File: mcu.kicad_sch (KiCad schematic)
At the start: 13 parts, among them U6 ATtiny3217

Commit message: Added labels and schematic PDF among other progress
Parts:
- U6: footprint Package_SO:TSSOP-20_4.4x6.5mm_P0.65mm -> Package_DFN_QFN:QFN-24-1EP_4x4mm_P0.5mm_EP2.6x2.6mm
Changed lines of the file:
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@@
 			)
 		)
-		(property "Footprint" "Package_SO:TSSOP-20_4.4x6.5mm_P0.65mm"
+		(property "Footprint" "Package_DFN_QFN:QFN-24-1EP_4x4mm_P0.5mm_EP2.6x2.6mm"
 			(at 133.35 133.35 0)
 			(hide yes)

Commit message: Added testpoints
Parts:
- added TP32: MCU_VCC, symbol Connector:TestPoint_Small
- renumbered C13 to C14, C14 to C15, R36 to R30, R38 to R31, R37 to R32, R30 to R33, R31 to R34, R32 to R35, R33 to R36, R34 to R37, R35 to R38, TP19 to TP33
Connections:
- net MCU_VCC: now also TP32.1
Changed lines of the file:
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@@
+	)
+	(junction
+		(at 133.35 82.55)
+		(diameter 0)
+		(color 0 0 0 0)
 	)
 	(junction
@@
 		(effects
 			(font
-				(size 1.27 1.27)
+				(size 1 1)
+				(thickness 0.254)
+				(bold yes)
 			)
 			(justify right bottom)
@@
 		(effects
 			(font
-				(size 1.27 1.27)
+				(size 1 1)
+				(thickness 0.2)
+				(bold yes)
 			)
 			(justify left bottom)
@@
 		(effects
 			(font
-				(size 1.27 1.27)
+				(size 1 1)
+				(thickness 0.2)
+				(bold yes)
 			)
 			(justify right bottom)
@@
 			(font
 				(size 1 1)
+				(thickness 0.2)
+				(bold yes)
 			)
 			(justify left bottom)
@@
 			(font
 				(size 1 1)
+				(thickness 0.2)
+				(bold yes)
 			)
 			(justify left bottom)
@@
 		(effects
 			(font
-				(size 1.27 1.27)
+				(size 1 1)
+				(thickness 0.2)
+				(bold yes)
 			)
 			(justify left bottom)
@@
 			(font
 				(size 1 1)
+				(thickness 0.2)
+				(bold yes)
 			)
 			(justify right bottom)
@@
 		(in_pos_files yes)
 		(dnp no)
-		(property "Reference" "R30"
+		(property "Reference" "R33"
 			(at 178.816 66.04 90)
 			(show_name no)
@@
 			(project "power_module"
 				(path "/33e2b92e-f705-4be7-96f4-57092b8ec1ea/20438595-580a-4bb7-878e-f4267085e0b4"
-					(reference "R30")
+					(reference "R33")
 					(unit 1)
 				)
@@
 		(in_pos_files yes)
 		(dnp no)
-		(property "Reference" "R37"
+		(property "Reference" "R32"
 			(at 180.34 127.254 0)
 			(show_name no)
@@
 			(project "power_module"
 				(path "/33e2b92e-f705-4be7-96f4-57092b8ec1ea/20438595-580a-4bb7-878e-f4267085e0b4"
-					(reference "R37")
+					(reference "R32")
 					(unit 1)
 				)
@@
 		(in_pos_files yes)
 		(dnp no)
-		(property "Reference" "C14"
+		(property "Reference" "C15"
 			(at 100.838 80.518 0)
 			(show_name no)
@@
 			(project "power_module"
 				(path "/33e2b92e-f705-4be7-96f4-57092b8ec1ea/20438595-580a-4bb7-878e-f4267085e0b4"
-					(reference "C14")
+					(reference "C15")
 					(unit 1)
 				)
@@
 		(in_pos_files yes)
 		(dnp no)
-		(property "Reference" "R33"
+		(property "Reference" "R36"
 			(at 179.578 84.836 90)
 			(show_name no)
@@
 			(project "power_module"
 				(path "/33e2b92e-f705-4be7-96f4-57092b8ec1ea/20438595-580a-4bb7-878e-f4267085e0b4"
-					(reference "R33")
+					(reference "R36")
 					(unit 1)
 				)
@@
 		(in_pos_files yes)
 		(dnp no)
-		(property "Reference" "R38"
+		(property "Reference" "R31"
 			(at 151.13 86.106 90)
 			(show_name no)
@@
 			(project "power_module"
 				(path "/33e2b92e-f705-4be7-96f4-57092b8ec1ea/20438595-580a-4bb7-878e-f4267085e0b4"
-					(reference "R38")
+					(reference "R31")
 					(unit 1)
 				)
@@
 		(in_pos_files yes)
 		(dnp no)
-		(property "Reference" "R35"
+		(property "Reference" "R38"
 			(at 179.832 100.076 90)
 			(show_name no)
@@
 			(project "power_module"
 				(path "/33e2b92e-f705-4be7-96f4-57092b8ec1ea/20438595-580a-4bb7-878e-f4267085e0b4"
-					(reference "R35")
+					(reference "R38")
 					(unit 1)
 				)
@@
 		(in_pos_files yes)
 		(dnp no)
-		(property "Reference" "TP19"
+		(property "Reference" "TP33"
 			(at 183.896 130.302 90)
 			(show_name no)
@@
 			(project "power_module"
 				(path "/33e2b92e-f705-4be7-96f4-57092b8ec1ea/20438595-580a-4bb7-878e-f4267085e0b4"
-					(reference "TP19")
+					(reference "TP33")
 					(unit 1)
 				)
@@
 		(in_pos_files yes)
 		(dnp no)
-		(property "Reference" "#PWR038"
+		(property "Reference" "#PWR040"
 			(at 91.44 91.44 0)
 			(hide yes)
@@
 			(project "power_module"
 				(path "/33e2b92e-f705-4be7-96f4-57092b8ec1ea/20438595-580a-4bb7-878e-f4267085e0b4"
-					(reference "#PWR038")
+					(reference "#PWR040")
 					(unit 1)
 				)
@@
 		(in_pos_files yes)
 		(dnp no)
-		(property "Reference" "C13"
+		(property "Reference" "C14"
 			(at 85.852 80.518 0)
 			(show_name no)
@@
 			(project "power_module"
 				(path "/33e2b92e-f705-4be7-96f4-57092b8ec1ea/20438595-580a-4bb7-878e-f4267085e0b4"
-					(reference "C13")
+					(reference "C14")
 					(unit 1)
 				)
@@
 		(in_pos_files yes)
 		(dnp no)
-		(property "Reference" "#PWR036"
+		(property "Reference" "#PWR041"
 			(at 133.35 78.74 0)
 			(hide yes)
@@
 			(project "power_module"
 				(path "/33e2b92e-f705-4be7-96f4-57092b8ec1ea/20438595-580a-4bb7-878e-f4267085e0b4"
-					(reference "#PWR036")
+					(reference "#PWR041")
 					(unit 1)
 				)
@@
 		(in_pos_files yes)
 		(dnp no)
-		(property "Reference" "R31"
+		(property "Reference" "R34"
 			(at 178.816 72.39 90)
 			(show_name no)
@@
 			(project "power_module"
 				(path "/33e2b92e-f705-4be7-96f4-57092b8ec1ea/20438595-580a-4bb7-878e-f4267085e0b4"
-					(reference "R31")
+					(reference "R34")
 					(unit 1)
 				)
@@
 		(in_pos_files yes)
 		(dnp no)
-		(property "Reference" "R34"
+		(property "Reference" "R37"
 			(at 179.578 91.186 90)
 			(show_name no)
@@
 			(project "power_module"
 				(path "/33e2b92e-f705-4be7-96f4-57092b8ec1ea/20438595-580a-4bb7-878e-f4267085e0b4"
-					(reference "R34")
+					(reference "R37")
+					(unit 1)
+				)
+			)
+		)
+	)
+	(symbol
+		(lib_id "Connector:TestPoint_Small")
+		(at 133.35 82.55 0)
+		(unit 1)
+		(body_style 1)
+		(exclude_from_sim no)
+		(in_bom yes)
+		(on_board yes)
+		(in_pos_files yes)
+		(dnp no)
+		(property "Reference" "TP32"
+			(at 133.858 82.042 0)
+			(show_name no)
+			(do_not_autoplace no)
+			(effects
+				(font
+					(size 1.27 1.27)
+				)
+				(justify left)
+			)
+		)
+		(property "Value" "MCU_VCC"
+			(at 134.62 83.8199 0)
+			(hide yes)
+			(show_name no)
+			(do_not_autoplace no)
+			(effects
+				(font
+					(size 1.27 1.27)
+				)
+				(justify left)
+			)
+		)
+		(property "Footprint" ""
+			(at 138.43 82.55 0)
+			(hide yes)
+			(show_name no)
+			(do_not_autoplace no)
+			(effects
+				(font
+					(size 1.27 1.27)
+				)
+			)
+		)
+		(property "Datasheet" ""
+			(at 138.43 82.55 0)
+			(hide yes)
+			(show_name no)
+			(do_not_autoplace no)
+			(effects
+				(font
+					(size 1.27 1.27)
+				)
+			)
+		)
+		(property "Description" "test point"
+			(at 133.35 82.55 0)
+			(hide yes)
+			(show_name no)
+			(do_not_autoplace no)
+			(effects
+				(font
+					(size 1.27 1.27)
+				)
+			)
+		)
+		(pin "1"
+		)
+		(instances
+			(project "power_module"
+				(path "/33e2b92e-f705-4be7-96f4-57092b8ec1ea/20438595-580a-4bb7-878e-f4267085e0b4"
+					(reference "TP32")
 					(unit 1)
 				)
@@
 		(in_pos_files yes)
 		(dnp no)
-		(property "Reference" "R32"
+		(property "Reference" "R35"
 			(at 179.324 80.772 90)
 			(show_name no)
@@
 			(project "power_module"
 				(path "/33e2b92e-f705-4be7-96f4-57092b8ec1ea/20438595-580a-4bb7-878e-f4267085e0b4"
-					(reference "R32")
+					(reference "R35")
 					(unit 1)
 				)
@@
 		(in_pos_files yes)
 		(dnp no)
-		(property "Reference" "#PWR037"
+		(property "Reference" "#PWR042"
 			(at 133.35 144.78 0)
 			(hide yes)
@@
 			(project "power_module"
 				(path "/33e2b92e-f705-4be7-96f4-57092b8ec1ea/20438595-580a-4bb7-878e-f4267085e0b4"
-					(reference "#PWR037")
+					(reference "#PWR042")
 					(unit 1)
 				)
@@
 		(in_pos_files yes)
 		(dnp no)
-		(property "Reference" "R36"
+		(property "Reference" "R30"
 			(at 132.334 77.216 0)
 			(show_name no)
@@
 			(project "power_module"
 				(path "/33e2b92e-f705-4be7-96f4-57092b8ec1ea/20438595-580a-4bb7-878e-f4267085e0b4"
-					(reference "R36")
+					(reference "R30")
 					(unit 1)
 				)

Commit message: Partially assigned netclasses WIP
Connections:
- net UDPI renamed UPDI
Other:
- moved on the sheet: R31
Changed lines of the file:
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@@
+	)
+	(junction
+		(at 175.26 132.08)
+		(diameter 0)
+		(color 0 0 0 0)
 	)
 	(junction
@@
 	)
 	(junction
-		(at 175.26 132.08)
-		(diameter 0)
-		(color 0 0 0 0)
-	)
-	(junction
 		(at 185.42 78.74)
 		(diameter 0)
@@
 	(wire
 		(pts
-			(xy 148.59 90.17) (xy 149.86 90.17)
+			(xy 148.59 90.17) (xy 151.13 90.17)
 		)
 		(stroke
@@
 		(pts
 			(xy 185.42 69.85) (xy 185.42 76.2)
-		)
-		(stroke
-			(width 0)
-			(type default)
-		)
-	)
-	(wire
-		(pts
-			(xy 157.48 90.17) (xy 158.75 90.17)
 		)
 		(stroke
@@
 		)
 	)
-	(hierarchical_label "UDPI"
+	(hierarchical_label "UPDI"
 		(shape bidirectional)
 		(at 158.75 90.17 0)
@@
 	(symbol
 		(lib_id "Device:R_US")
-		(at 153.67 90.17 90)
+		(at 154.94 90.17 90)
 		(mirror x)
 		(unit 1)
@@
 		(dnp no)
 		(property "Reference" "R31"
-			(at 151.13 86.106 90)
+			(at 152.4 86.106 90)
 			(show_name no)
 			(do_not_autoplace no)
@@
 		)
 		(property "Value" "100R"
-			(at 151.384 88.138 90)
+			(at 152.654 88.138 90)
 			(show_name no)
 			(do_not_autoplace no)
@@
 		)
 		(property "Footprint" "Resistor_SMD:R_0603_1608Metric"
-			(at 153.924 91.186 90)
+			(at 155.194 91.186 90)
 			(hide yes)
 			(show_name no)
@@
 		)
 		(property "Datasheet" ""
-			(at 153.67 90.17 0)
+			(at 154.94 90.17 0)
 			(hide yes)
 			(show_name no)
@@
 		)
 		(property "Description" "Resistor, US symbol"
-			(at 153.67 90.17 0)
+			(at 154.94 90.17 0)
 			(hide yes)
 			(show_name no)
@@
 		)
 		(property "MFR#" "RC0603FR-07100RL"
-			(at 153.67 90.17 0)
+			(at 154.94 90.17 0)
 			(hide yes)
 			(show_name no)
@@
 		)
 		(property "Package" "0603"
-			(at 153.67 90.17 0)
+			(at 154.94 90.17 0)
 			(hide yes)
 			(show_name no)
@@
 		)
 		(property "LCSC#" "C105588"
-			(at 153.67 90.17 0)
-			(hide yes)
-			(show_name no)
+			(at 154.94 90.17 0)
+			(hide yes)
+			(show_name no)

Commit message: Configured Varients
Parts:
- renumbered R30 to R31, R31 to R32, R32 to R33, R33 to R34, R34 to R35, R35 to R36, R36 to R37, R37 to R38, R38 to R39
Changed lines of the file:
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@@
 		(in_pos_files yes)
 		(dnp no)
-		(property "Reference" "R33"
+		(property "Reference" "R34"
 			(at 178.816 66.04 90)
 			(show_name no)
@@
 			(project "power_module"
 				(path "/33e2b92e-f705-4be7-96f4-57092b8ec1ea/20438595-580a-4bb7-878e-f4267085e0b4"
-					(reference "R33")
+					(reference "R34")
 					(unit 1)
+					(variant
+						(name "3v3 Dumb")
+						(dnp yes)
+					)
+					(variant
+						(name "5v Dumb")
+						(dnp yes)
+					)
 				)
 			)
@@
 		(in_pos_files yes)
 		(dnp no)
-		(property "Reference" "R32"
+		(property "Reference" "R33"
 			(at 180.34 127.254 0)
 			(show_name no)
@@
 			(project "power_module"
 				(path "/33e2b92e-f705-4be7-96f4-57092b8ec1ea/20438595-580a-4bb7-878e-f4267085e0b4"
-					(reference "R32")
+					(reference "R33")
 					(unit 1)
+					(variant
+						(name "3v3 Dumb")
+						(dnp yes)
+					)
+					(variant
+						(name "5v Dumb")
+						(dnp yes)
+					)
 				)
 			)
@@
 					(reference "C15")
 					(unit 1)
+					(variant
+						(name "3v3 Dumb")
+						(dnp yes)
+					)
+					(variant
+						(name "5v Dumb")
+						(dnp yes)
+					)
 				)
 			)
@@
 		(in_pos_files yes)
 		(dnp no)
-		(property "Reference" "R36"
+		(property "Reference" "R37"
 			(at 179.578 84.836 90)
 			(show_name no)
@@
 			(project "power_module"
 				(path "/33e2b92e-f705-4be7-96f4-57092b8ec1ea/20438595-580a-4bb7-878e-f4267085e0b4"
-					(reference "R36")
+					(reference "R37")
 					(unit 1)
+					(variant
+						(name "3v3 Dumb")
+						(dnp yes)
+					)
+					(variant
+						(name "5v Dumb")
+						(dnp yes)
+					)
 				)
 			)
@@
 		(in_pos_files yes)
 		(dnp no)
-		(property "Reference" "R31"
+		(property "Reference" "R32"
 			(at 152.4 86.106 90)
 			(show_name no)
@@
 			(project "power_module"
 				(path "/33e2b92e-f705-4be7-96f4-57092b8ec1ea/20438595-580a-4bb7-878e-f4267085e0b4"
-					(reference "R31")
+					(reference "R32")
 					(unit 1)
 				)
@@
 		(in_pos_files yes)
 		(dnp no)
-		(property "Reference" "R38"
+		(property "Reference" "R39"
 			(at 179.832 100.076 90)
 			(show_name no)
@@
 			(project "power_module"
 				(path "/33e2b92e-f705-4be7-96f4-57092b8ec1ea/20438595-580a-4bb7-878e-f4267085e0b4"
-					(reference "R38")
+					(reference "R39")
 					(unit 1)
+					(variant
+						(name "3v3 Dumb")
+						(dnp yes)
+					)
+					(variant
+						(name "5v Dumb")
+						(dnp yes)
+					)
 				)
 			)
@@
 					(reference "C14")
 					(unit 1)
+					(variant
+						(name "3v3 Dumb")
+						(dnp yes)
+					)
+					(variant
+						(name "5v Dumb")
+						(dnp yes)
+					)
 				)
 			)
@@
 		(in_pos_files yes)
 		(dnp no)
-		(property "Reference" "R34"
+		(property "Reference" "R35"
 			(at 178.816 72.39 90)
 			(show_name no)
@@
 			(project "power_module"
 				(path "/33e2b92e-f705-4be7-96f4-57092b8ec1ea/20438595-580a-4bb7-878e-f4267085e0b4"
-					(reference "R34")
+					(reference "R35")
 					(unit 1)
+					(variant
+						(name "3v3 Dumb")
+						(dnp yes)
+					)
+					(variant
+						(name "5v Dumb")
+						(dnp yes)
+					)
 				)
 			)
@@
 		(in_pos_files yes)
 		(dnp no)
-		(property "Reference" "R37"
+		(property "Reference" "R38"
 			(at 179.578 91.186 90)
 			(show_name no)
@@
 			(project "power_module"
 				(path "/33e2b92e-f705-4be7-96f4-57092b8ec1ea/20438595-580a-4bb7-878e-f4267085e0b4"
-					(reference "R37")
+					(reference "R38")
 					(unit 1)
+					(variant
+						(name "3v3 Dumb")
+						(dnp yes)
+					)
+					(variant
+						(name "5v Dumb")
+						(dnp yes)
+					)
 				)
 			)
@@
 		(in_pos_files yes)
 		(dnp no)
-		(property "Reference" "R35"
+		(property "Reference" "R36"
 			(at 179.324 80.772 90)
 			(show_name no)
@@
 			(project "power_module"
 				(path "/33e2b92e-f705-4be7-96f4-57092b8ec1ea/20438595-580a-4bb7-878e-f4267085e0b4"
-					(reference "R35")
+					(reference "R36")
 					(unit 1)
+					(variant
+						(name "3v3 Dumb")
+						(dnp yes)
+					)
+					(variant
+						(name "5v Dumb")
+						(dnp yes)
+					)
 				)
 			)
@@
 		(in_pos_files yes)
 		(dnp no)
-		(property "Reference" "R30"
+		(property "Reference" "R31"
 			(at 132.334 77.216 0)
 			(show_name no)
@@
 			(project "power_module"
 				(path "/33e2b92e-f705-4be7-96f4-57092b8ec1ea/20438595-580a-4bb7-878e-f4267085e0b4"
-					(reference "R30")
+					(reference "R31")
 					(unit 1)
+					(variant
+						(name "3v3 Dumb")
+						(dnp yes)
+					)
+					(variant
+						(name "5v Dumb")
+						(dnp yes)
+					)
 				)
 			)
@@
 					(reference "U6")
 					(unit 1)
-				)
-			)
+					(variant
+						(name "3v3 Dumb")
+						(dnp yes)
+					)
+					(variant
+						(name "5v Dumb")
+						(dnp yes)
+					)
+				)
+			)

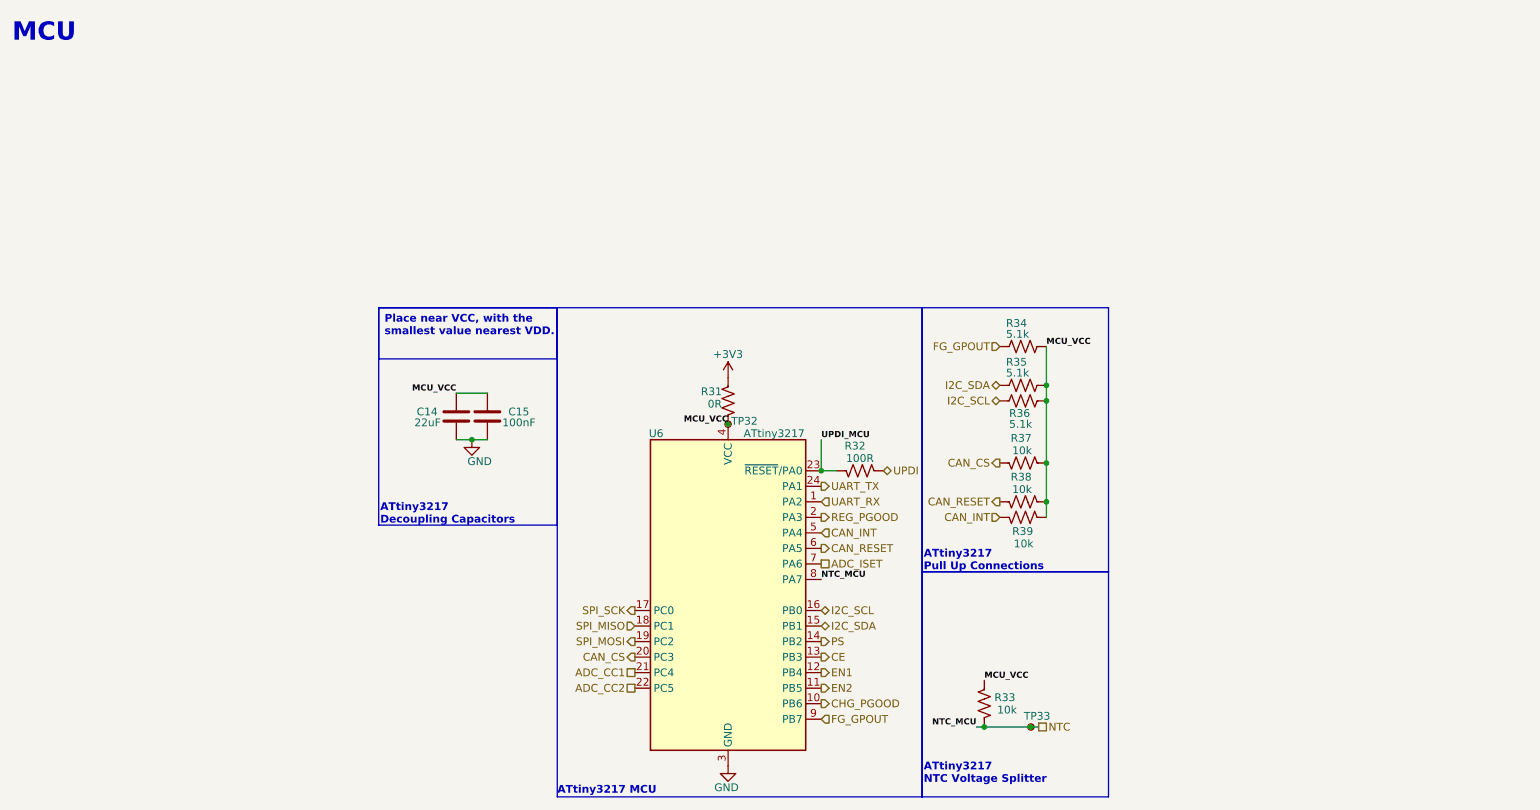
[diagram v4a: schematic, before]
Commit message: Started work on PCB layout
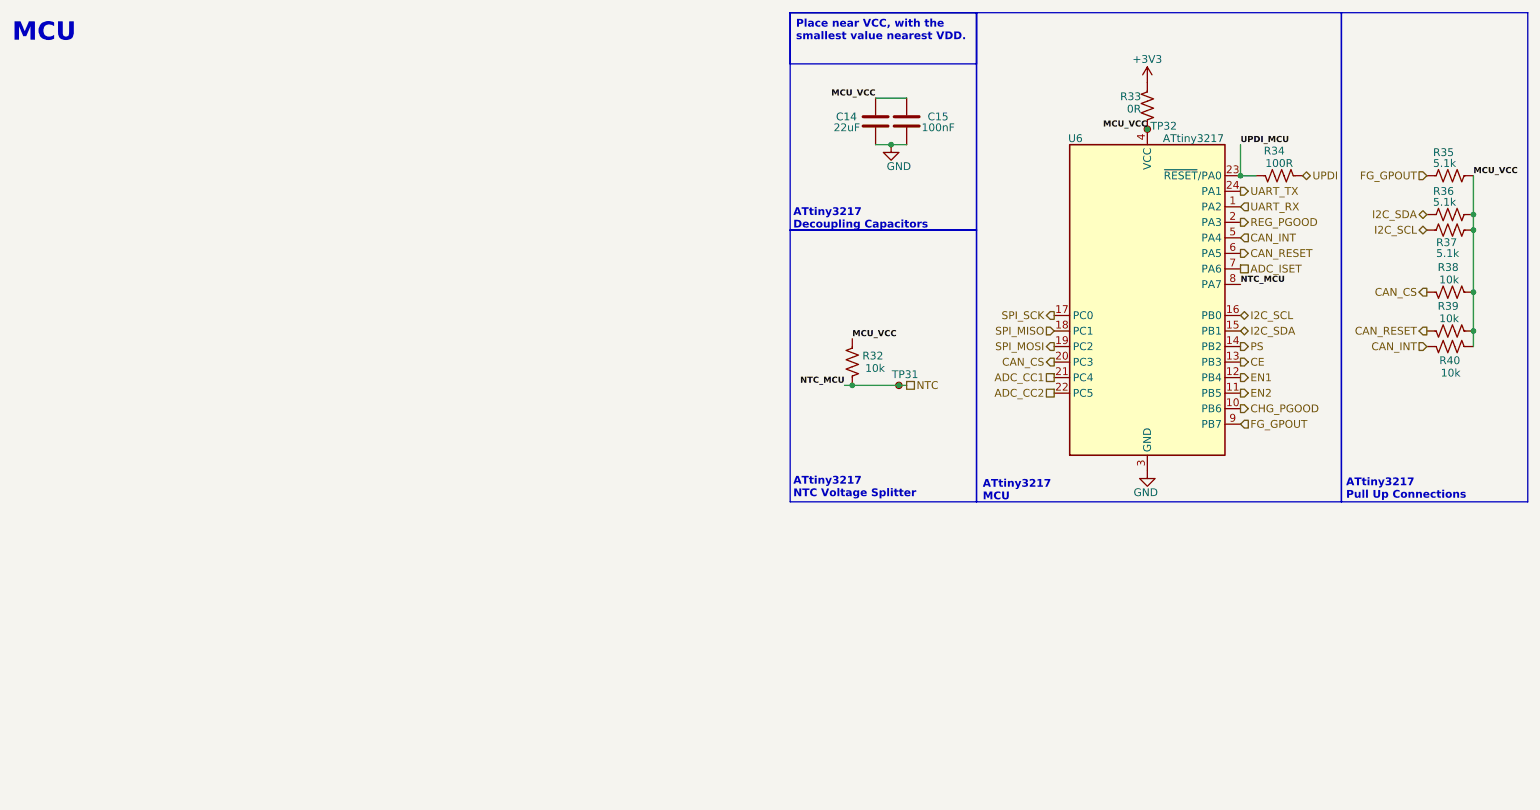
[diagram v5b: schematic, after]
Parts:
- TP32: footprint (none) -> TestPoint:TestPoint_Pad_D1.0mm
- renumbered R33 to R32, R31 to R33, R32 to R34, R34 to R35, R35 to R36, R36 to R37, R37 to R38, R38 to R39, R39 to R40, TP33 to TP31
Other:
- moved on the sheet: C14, C15, R32, R33, R34, R35, R36, R37, R38, R39, R40, TP31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
